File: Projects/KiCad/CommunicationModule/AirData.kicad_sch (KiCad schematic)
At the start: 24 parts, among them J1 Conn_01x04_Pin, J2 Conn_01x04_Pin, SW1 SW_Push, U1 ABX00012, U2 MCP2562-E-P, U3 MCP2515-I/P, Y1 8MHz

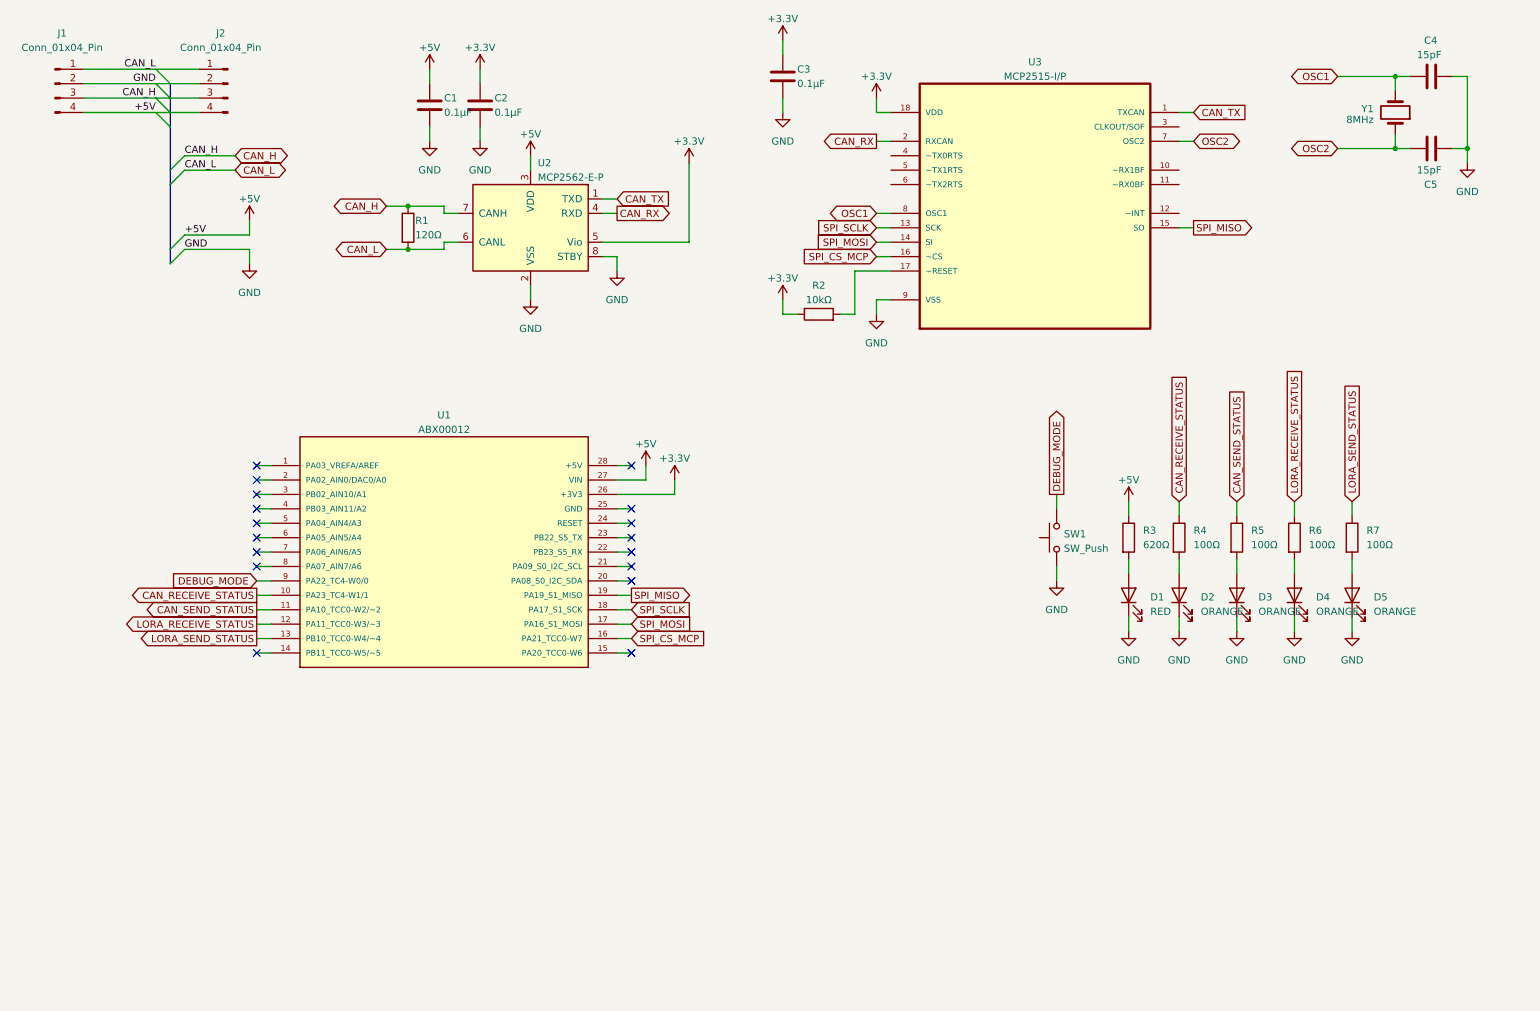
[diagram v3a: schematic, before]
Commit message: コネクタを再配置, 基板上で12V->5Vをするように変更
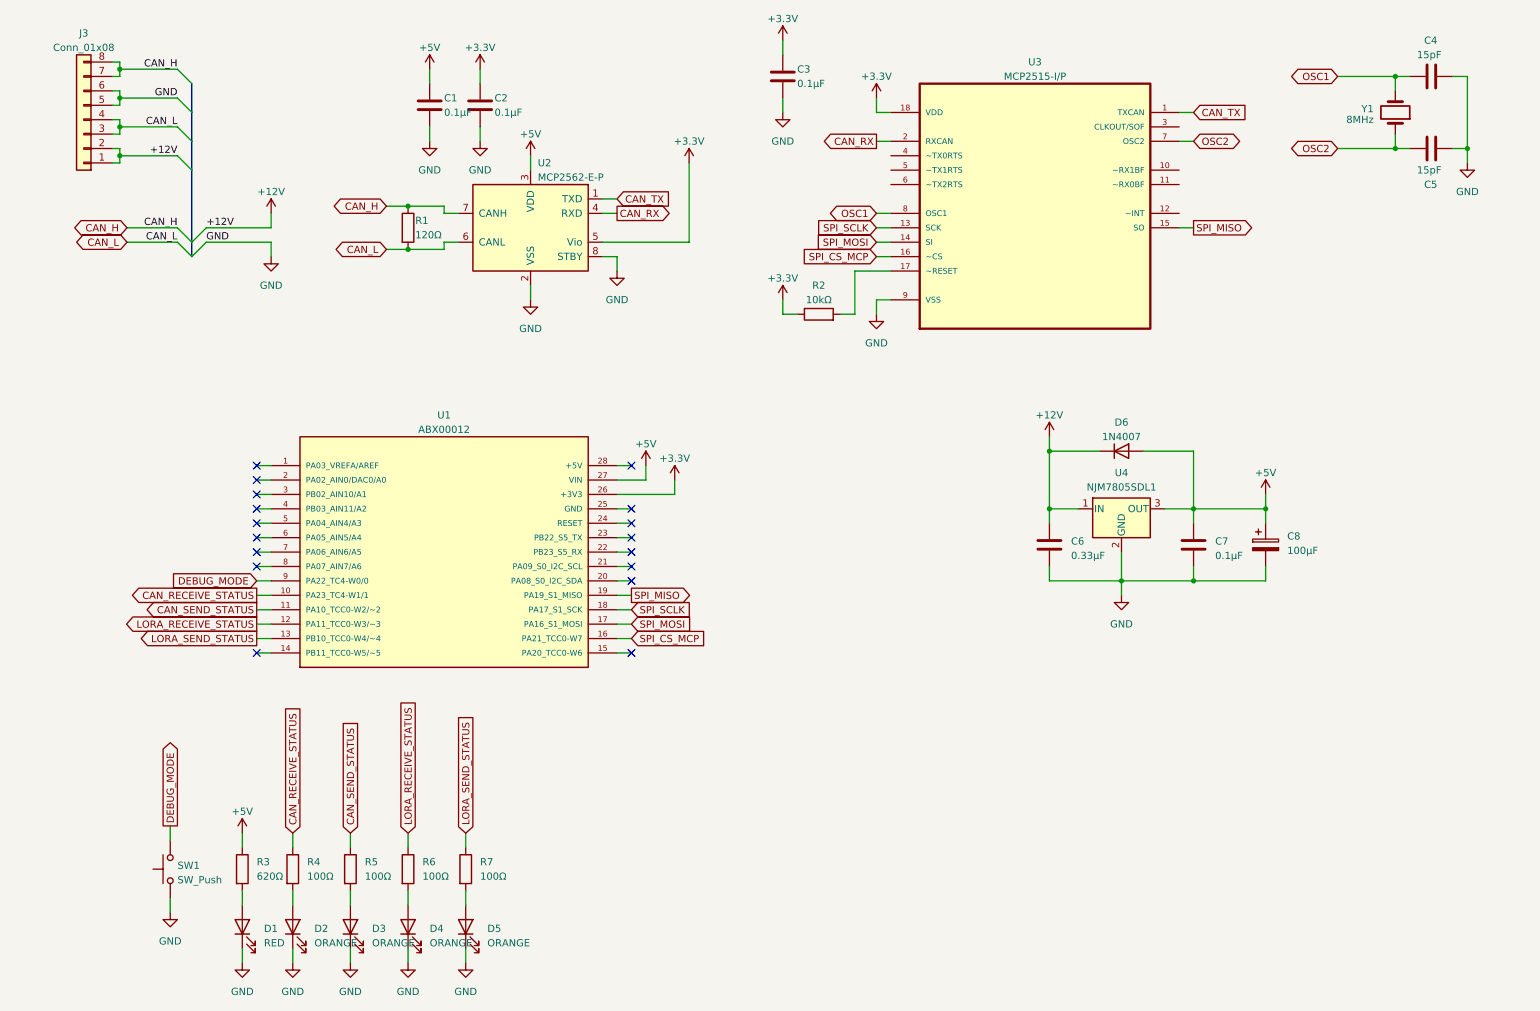
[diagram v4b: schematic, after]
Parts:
- removed J1, J2: Conn_01x04_Pin, Connector_JST:JST_XH_S4B-XH-A_1x04_P2.50mm_Horizontal, symbol Connector:Conn_01x04_Pin
- added C6: 0.33μF, Capacitor_SMD:C_0805_2012Metric_Pad1.18x1.45mm_HandSolder, symbol Device:C
- added C7: 0.1μF, Capacitor_SMD:C_0805_2012Metric_Pad1.18x1.45mm_HandSolder, symbol Device:C
- added C8: 100μF, Capacitor_SMD:CP_Elec_6.3x7.7, symbol Device:C_Polarized
- added D6: 1N4007, Diode_SMD:D_SOD-123F, symbol Diode:1N4007
- added J3: Conn_01x08, Connector_Hirose:Hirose_DF11-8DP-2DSA_2x04_P2.00mm_Vertical, symbol Connector_Generic:Conn_01x08
- added U4: NJM7805SDL1, Package_TO_SOT_SMD:TO-252-3_TabPin2, symbol Regulator_Linear:L7805
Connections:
- net +5V: now also C7.1, C8.1, D6.2 (A), U4.3 (OUT)
- net CAN_H: now also J3.7 (Pin_7), J3.8 (Pin_8)
- net CAN_L: now also J3.3 (Pin_3), J3.4 (Pin_4)
- net GND: now also C6.2, C7.2, C8.2, J3.5 (Pin_5), J3.6 (Pin_6), U4.2 (GND)
- new net +12V: C6.1, D6.1 (K), J3.1 (Pin_1), J3.2 (Pin_2), U4.1 (IN)
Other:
- moved on the sheet: D1, D2, D3, D4, D5, R3, R4, R5, R6, R7, SW1

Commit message: 基板設計の都市伝説をいろいろ適応
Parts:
- U4: renamed from U1; footprint ARDUINO_ABX00012 -> ABX00012:ARDUINO_ABX00012
- renumbered C4 to C1, C6 to C2, C2 to C3, C1 to C4, C3 to C5, C7 to C6, C5 to C7, D3 to D2, D2 to D3, D6 to D4, D4 to D5, D5 to D6, J3 to J1, R3 to R2, R2 to R3, U2 to U1, U3 to U2, U4 to U3
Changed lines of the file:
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@@
   (symbol (lib_id "Device:LED") (at 93.98 176.53 90) (unit 1)
     (in_bom yes) (on_board yes) (dnp no) (fields_autoplaced)
-    (property "Reference" "D5" (at 97.79 176.8474 90)
+    (property "Reference" "D6" (at 97.79 176.8474 90)
       (effects (font (size 1.27 1.27)) (justify right))
     )
@@
       (project "AirData"
         (path "/ea1ed597-7cd3-4340-902e-bdce8f2d7a62"
-          (reference "D5") (unit 1)
+          (reference "D6") (unit 1)
         )
       )
@@
   (symbol (lib_id "Device:LED") (at 63.5 176.53 90) (unit 1)
     (in_bom yes) (on_board yes) (dnp no) (fields_autoplaced)
-    (property "Reference" "D2" (at 67.31 176.8474 90)
+    (property "Reference" "D3" (at 67.31 176.8474 90)
       (effects (font (size 1.27 1.27)) (justify right))
     )
@@
       (project "AirData"
         (path "/ea1ed597-7cd3-4340-902e-bdce8f2d7a62"
-          (reference "D2") (unit 1)
+          (reference "D3") (unit 1)
         )
       )
@@
   (symbol (lib_id "Device:R") (at 156.21 68.58 90) (unit 1)
     (in_bom yes) (on_board yes) (dnp no) (fields_autoplaced)
-    (property "Reference" "R2" (at 156.21 63.5 90)
+    (property "Reference" "R3" (at 156.21 63.5 90)
       (effects (font (size 1.27 1.27)))
     )
@@
       (project "AirData"
         (path "/ea1ed597-7cd3-4340-902e-bdce8f2d7a62"
-          (reference "R2") (unit 1)
+          (reference "R3") (unit 1)
         )
       )
@@
   (symbol (lib_id "Device:C") (at 264.16 39.37 270) (mirror x) (unit 1)
     (in_bom yes) (on_board yes) (dnp no)
-    (property "Reference" "C5" (at 262.89 45.72 90)
+    (property "Reference" "C7" (at 262.89 45.72 90)
       (effects (font (size 1.27 1.27)) (justify left))
     )
@@
       (project "AirData"
         (path "/ea1ed597-7cd3-4340-902e-bdce8f2d7a62"
-          (reference "C5") (unit 1)
+          (reference "C7") (unit 1)
         )
       )
@@
   (symbol (lib_id "Regulator_Linear:L7805") (at 209.55 102.87 0) (unit 1)
     (in_bom yes) (on_board yes) (dnp no) (fields_autoplaced)
-    (property "Reference" "U4" (at 209.55 96.52 0)
+    (property "Reference" "U3" (at 209.55 96.52 0)
       (effects (font (size 1.27 1.27)))
     )
@@
       (project "AirData"
         (path "/ea1ed597-7cd3-4340-902e-bdce8f2d7a62"
-          (reference "U4") (unit 1)
+          (reference "U3") (unit 1)
         )
       )
@@
   (symbol (lib_id "Device:C") (at 96.52 31.75 0) (unit 1)
     (in_bom yes) (on_board yes) (dnp no)
-    (property "Reference" "C2" (at 99.06 30.48 0)
+    (property "Reference" "C3" (at 99.06 30.48 0)
       (effects (font (size 1.27 1.27)) (justify left))
     )
@@
       (project "AirData"
         (path "/ea1ed597-7cd3-4340-902e-bdce8f2d7a62"
-          (reference "C2") (unit 1)
+          (reference "C3") (unit 1)
         )
       )
@@
   (symbol (lib_id "Device:LED") (at 83.82 176.53 90) (unit 1)
     (in_bom yes) (on_board yes) (dnp no) (fields_autoplaced)
-    (property "Reference" "D4" (at 87.63 176.8474 90)
+    (property "Reference" "D5" (at 87.63 176.8474 90)
       (effects (font (size 1.27 1.27)) (justify right))
     )
@@
       (project "AirData"
         (path "/ea1ed597-7cd3-4340-902e-bdce8f2d7a62"
-          (reference "D4") (unit 1)
+          (reference "D5") (unit 1)
         )
       )
@@
   (symbol (lib_id "Interface_CAN_LIN:MCP2562-E-P") (at 105.41 53.34 0) (mirror y) (unit 1)
     (in_bom yes) (on_board yes) (dnp no)
-    (property "Reference" "U2" (at 106.68 41.91 0)
+    (property "Reference" "U1" (at 106.68 41.91 0)
       (effects (font (size 1.27 1.27)) (justify right))
     )
@@
       (project "AirData"
         (path "/ea1ed597-7cd3-4340-902e-bdce8f2d7a62"
-          (reference "U2") (unit 1)
+          (reference "U1") (unit 1)
         )
       )
@@
   (symbol (lib_id "Device:C") (at 149.86 26.67 0) (unit 1)
     (in_bom yes) (on_board yes) (dnp no)
-    (property "Reference" "C3" (at 152.4 25.4 0)
+    (property "Reference" "C5" (at 152.4 25.4 0)
       (effects (font (size 1.27 1.27)) (justify left))
     )
@@
       (project "AirData"
         (path "/ea1ed597-7cd3-4340-902e-bdce8f2d7a62"
-          (reference "C3") (unit 1)
+          (reference "C5") (unit 1)
         )
       )
@@
   (symbol (lib_id "Device:C") (at 87.63 31.75 0) (unit 1)
     (in_bom yes) (on_board yes) (dnp no)
-    (property "Reference" "C1" (at 90.17 30.48 0)
+    (property "Reference" "C4" (at 90.17 30.48 0)
       (effects (font (size 1.27 1.27)) (justify left))
     )
@@
       (project "AirData"
         (path "/ea1ed597-7cd3-4340-902e-bdce8f2d7a62"
-          (reference "C1") (unit 1)
+          (reference "C4") (unit 1)
         )
       )
@@
   (symbol (lib_id "Device:C") (at 222.25 109.22 0) (unit 1)
     (in_bom yes) (on_board yes) (dnp no) (fields_autoplaced)
-    (property "Reference" "C7" (at 226.06 108.585 0)
+    (property "Reference" "C6" (at 226.06 108.585 0)
       (effects (font (size 1.27 1.27)) (justify left))
     )
@@
       (project "AirData"
         (path "/ea1ed597-7cd3-4340-902e-bdce8f2d7a62"
-          (reference "C7") (unit 1)
+          (reference "C6") (unit 1)
         )
       )
@@
   (symbol (lib_id "ABX00012:ABX00012") (at 90.17 110.49 0) (unit 1)
     (in_bom yes) (on_board yes) (dnp no) (fields_autoplaced)
-    (property "Reference" "U1" (at 90.17 86.36 0)
+    (property "Reference" "U4" (at 90.17 86.36 0)
       (effects (font (size 1.27 1.27)))
     )
@@
       (effects (font (size 1.27 1.27)))
     )
-    (property "Footprint" "ARDUINO_ABX00012" (at 90.17 110.49 0)
+    (property "Footprint" "ABX00012:ARDUINO_ABX00012" (at 90.17 110.49 0)
       (effects (font (size 1.27 1.27)) (justify bottom) hide)
     )
@@
       (project "AirData"
         (path "/ea1ed597-7cd3-4340-902e-bdce8f2d7a62"
-          (reference "U1") (unit 1)
+          (reference "U4") (unit 1)
         )
       )
@@
   (symbol (lib_id "Device:C") (at 196.85 109.22 0) (unit 1)
     (in_bom yes) (on_board yes) (dnp no) (fields_autoplaced)
-    (property "Reference" "C6" (at 200.66 108.585 0)
+    (property "Reference" "C2" (at 200.66 108.585 0)
       (effects (font (size 1.27 1.27)) (justify left))
     )
@@
       (project "AirData"
         (path "/ea1ed597-7cd3-4340-902e-bdce8f2d7a62"
-          (reference "C6") (unit 1)
+          (reference "C2") (unit 1)
         )
       )
@@
   (symbol (lib_id "MCP2515-I_P:MCP2515-I{slash}P") (at 194.31 45.72 0) (unit 1)
     (in_bom yes) (on_board yes) (dnp no) (fields_autoplaced)
-    (property "Reference" "U3" (at 194.31 24.13 0)
+    (property "Reference" "U2" (at 194.31 24.13 0)
       (effects (font (size 1.27 1.27)))
     )
@@
       (project "AirData"
         (path "/ea1ed597-7cd3-4340-902e-bdce8f2d7a62"
-          (reference "U3") (unit 1)
+          (reference "U2") (unit 1)
         )
       )
@@
   (symbol (lib_id "Device:R") (at 54.61 166.37 0) (unit 1)
     (in_bom yes) (on_board yes) (dnp no) (fields_autoplaced)
-    (property "Reference" "R3" (at 57.15 165.0999 0)
+    (property "Reference" "R2" (at 57.15 165.0999 0)
       (effects (font (size 1.27 1.27)) (justify left))
     )
@@
       (project "AirData"
         (path "/ea1ed597-7cd3-4340-902e-bdce8f2d7a62"
-          (reference "R3") (unit 1)
+          (reference "R2") (unit 1)
         )
       )
@@
   (symbol (lib_id "Device:C") (at 264.16 26.67 270) (mirror x) (unit 1)
     (in_bom yes) (on_board yes) (dnp no)
-    (property "Reference" "C4" (at 262.89 20.32 90)
+    (property "Reference" "C1" (at 262.89 20.32 90)
       (effects (font (size 1.27 1.27)) (justify left))
     )
@@
       (project "AirData"
         (path "/ea1ed597-7cd3-4340-902e-bdce8f2d7a62"
-          (reference "C4") (unit 1)
+          (reference "C1") (unit 1)
         )
       )
@@
   (symbol (lib_id "Device:LED") (at 73.66 176.53 90) (unit 1)
     (in_bom yes) (on_board yes) (dnp no) (fields_autoplaced)
-    (property "Reference" "D3" (at 77.47 176.8474 90)
+    (property "Reference" "D2" (at 77.47 176.8474 90)
       (effects (font (size 1.27 1.27)) (justify right))
     )
@@
       (project "AirData"
         (path "/ea1ed597-7cd3-4340-902e-bdce8f2d7a62"
-          (reference "D3") (unit 1)
+          (reference "D2") (unit 1)
         )
       )
@@
   (symbol (lib_id "Diode:1N4007") (at 209.55 92.71 0) (unit 1)
     (in_bom yes) (on_board yes) (dnp no) (fields_autoplaced)
-    (property "Reference" "D6" (at 209.55 87.63 0)
+    (property "Reference" "D4" (at 209.55 87.63 0)
       (effects (font (size 1.27 1.27)))
     )
@@
       (project "AirData"
         (path "/ea1ed597-7cd3-4340-902e-bdce8f2d7a62"
-          (reference "D6") (unit 1)
+          (reference "D4") (unit 1)
         )
       )
@@
   (symbol (lib_id "Connector_Generic:Conn_01x08") (at 26.67 34.29 180) (unit 1)
     (in_bom yes) (on_board yes) (dnp no) (fields_autoplaced)
-    (property "Reference" "J3" (at 26.67 19.05 0)
+    (property "Reference" "J1" (at 26.67 19.05 0)
       (effects (font (size 1.27 1.27)))
     )
@@
       (project "AirData"
         (path "/ea1ed597-7cd3-4340-902e-bdce8f2d7a62"
-          (reference "J3") (unit 1)
-        )
-      )
+          (reference "J1") (unit 1)
+        )
+      )

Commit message: テストポイントを追加
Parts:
- added TP1, TP2: TestPoint, Connector_Pin:Pin_D1.0mm_L10.0mm, symbol Connector:TestPoint
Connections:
- net CAN_H: now also TP1.1
- net CAN_L: now also TP2.1
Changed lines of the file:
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@@
+    )
+  )
+  (symbol (lib_id "Connector:TestPoint") (at 83.82 57.15 180) (unit 1)
+    (in_bom yes) (on_board yes) (dnp no) (fields_autoplaced)
+    (property "Reference" "TP2" (at 86.36 59.817 0)
+      (effects (font (size 1.27 1.27)) (justify right))
+    )
+    (property "Value" "TestPoint" (at 86.36 62.357 0)
+      (effects (font (size 1.27 1.27)) (justify right))
+    )
+    (property "Footprint" "Connector_Pin:Pin_D1.0mm_L10.0mm" (at 78.74 57.15 0)
+      (effects (font (size 1.27 1.27)) hide)
+    )
+    (property "Datasheet" "~" (at 78.74 57.15 0)
+      (effects (font (size 1.27 1.27)) hide)
+    )
+    (pin "1")
+    (instances
+      (project "AirData"
+        (path "/ea1ed597-7cd3-4340-902e-bdce8f2d7a62"
+          (reference "TP2") (unit 1)
+        )
+      )
     )
   )
@@
         )
       )
+    )
+  )
+  (symbol (lib_id "Connector:TestPoint") (at 83.82 49.53 0) (unit 1)
+    (in_bom yes) (on_board yes) (dnp no) (fields_autoplaced)
+    (property "Reference" "TP1" (at 86.36 45.593 0)
+      (effects (font (size 1.27 1.27)) (justify left))
+    )
+    (property "Value" "TestPoint" (at 86.36 48.133 0)
+      (effects (font (size 1.27 1.27)) (justify left))
+    )
+    (property "Footprint" "Connector_Pin:Pin_D1.0mm_L10.0mm" (at 88.9 49.53 0)
+      (effects (font (size 1.27 1.27)) hide)
+    )
+    (property "Datasheet" "~" (at 88.9 49.53 0)
+      (effects (font (size 1.27 1.27)) hide)
+    )
+    (pin "1")
+    (instances
+      (project "AirData"
+        (path "/ea1ed597-7cd3-4340-902e-bdce8f2d7a62"
+          (reference "TP1") (unit 1)
+        )
+      )
